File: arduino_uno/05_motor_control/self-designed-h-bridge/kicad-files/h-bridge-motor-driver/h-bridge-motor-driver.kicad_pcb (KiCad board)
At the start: 2 copper layers, 1 part

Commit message: rework pcb
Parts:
- removed REF**: CONN2_2601-3102_WAG, WAGO 2601-3102:CONN2_2601-3102_WAG
- added D1: 1N4007, Diode_THT:D_DO-41_SOD81_P10.16mm_Horizontal, F.Cu at (104.5, 66.8)
- added D2: 1N4007, Diode_THT:D_DO-41_SOD81_P10.16mm_Horizontal, F.Cu at (104.5, 71.0)
- added D3: 1N4007, Diode_THT:D_DO-41_SOD81_P10.16mm_Horizontal, F.Cu at (104.5, 75.3)
- added D4: 1N4007, Diode_THT:D_DO-41_SOD81_P10.16mm_Horizontal, F.Cu at (104.5, 79.5)
- added J1: Conn_01x05_Pin, Connector_PinHeader_2.54mm:PinHeader_1x05_P2.54mm_Vertical, F.Cu at (118.8, 67.0)
- added J3: 2601-3102, WAGO 2601-3102:CONN2_2601-3102_WAG, F.Cu at (108.1, 56.5)
- added J4: 2601-3102, WAGO 2601-3102:CONN2_2601-3102_WAG, F.Cu at (266.0, 53.0)
- added Q1: IRF9540N, Package_TO_SOT_THT:TO-220-3_Vertical, F.Cu at (105.9, 85.6)
- added Q2: IRLIZ44N, Package_TO_SOT_THT:TO-220F-3_Vertical, F.Cu at (119.9, 83.2)
- added Q3: IRF9540N, Package_TO_SOT_THT:TO-220-3_Vertical, F.Cu at (105.9, 91.5)
- added Q4: IRLIZ44N, Package_TO_SOT_THT:TO-220F-3_Vertical, F.Cu at (119.9, 89.5)
- added Q5: BC547, Package_TO_SOT_THT:TO-92_Inline, F.Cu at (123.1, 67.9)
- added Q6: BC547, Package_TO_SOT_THT:TO-92_Inline, F.Cu at (123.1, 73.7)
- added R1: 330, Resistor_THT:R_Axial_DIN0207_L6.3mm_D2.5mm_P10.16mm_Horizontal, F.Cu at (90.9, 52.3)
- added R2: 10k, Resistor_THT:R_Axial_DIN0207_L6.3mm_D2.5mm_P10.16mm_Horizontal, F.Cu at (90.9, 56.3)
- added R3: 10k, Resistor_THT:R_Axial_DIN0207_L6.3mm_D2.5mm_P10.16mm_Horizontal, F.Cu at (90.9, 60.4)
- added R4: 330, Resistor_THT:R_Axial_DIN0207_L6.3mm_D2.5mm_P10.16mm_Horizontal, F.Cu at (90.9, 64.4)
- added R5: 330, Resistor_THT:R_Axial_DIN0207_L6.3mm_D2.5mm_P10.16mm_Horizontal, F.Cu at (90.9, 68.5)
- added R6: 330, Resistor_THT:R_Axial_DIN0207_L6.3mm_D2.5mm_P10.16mm_Horizontal, F.Cu at (90.9, 72.5)
- added R7: 10k, Resistor_THT:R_Axial_DIN0207_L6.3mm_D2.5mm_P10.16mm_Horizontal, F.Cu at (90.9, 76.6)
- added R8: 10k, Resistor_THT:R_Axial_DIN0207_L6.3mm_D2.5mm_P10.16mm_Horizontal, F.Cu at (90.9, 80.6)

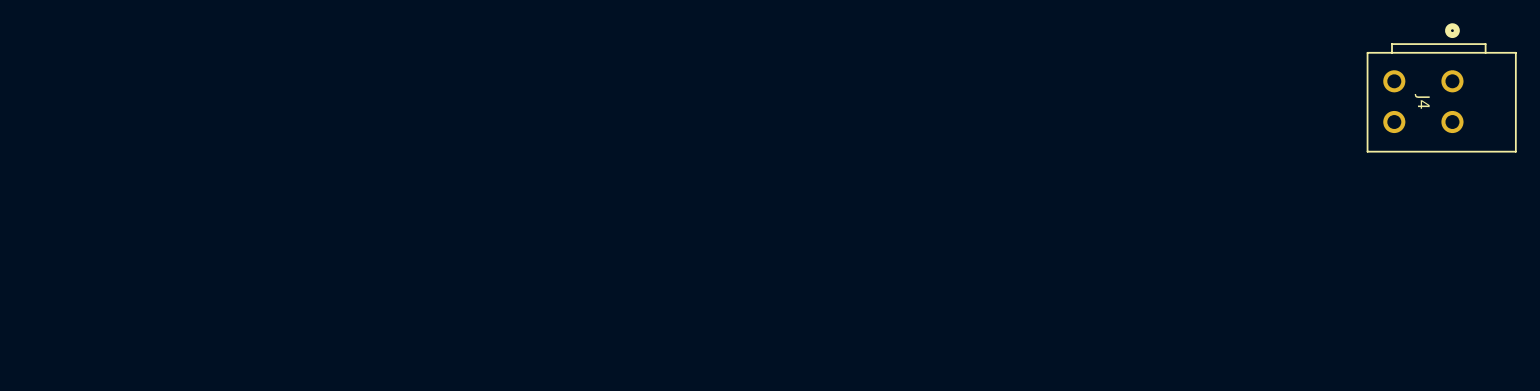
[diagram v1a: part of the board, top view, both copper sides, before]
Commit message: add 3d model to wago connector
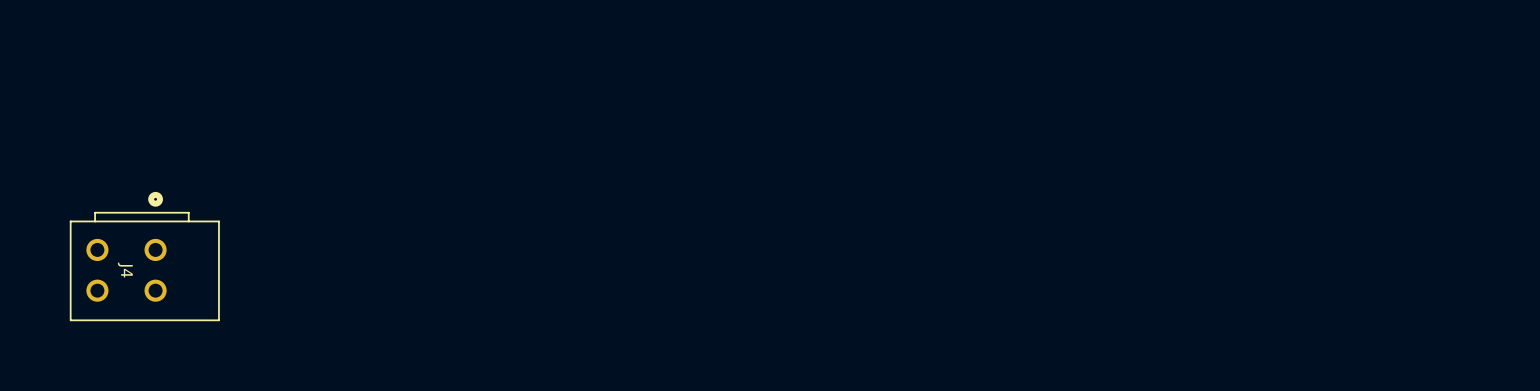
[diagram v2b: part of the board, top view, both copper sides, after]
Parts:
- moved J4 112.4 mm to (154.5, 67.5)
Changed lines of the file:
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@@
 		)
 		(embedded_fonts no)
+		(model "C:/workspace/PycharmProjects/arduino_projects/arduino_uno/05_motor_control/self-designed-h-bridge/kicad-files/part-models/wago-2601-3102/2601-3102.stp"
+			(offset
+				(xyz 4.5 -5 0)
+			)
+			(scale
+				(xyz 1 1 1)
+			)
+			(rotate
+				(xyz -90 -0 90)
+			)
+		)
 	)
 	(footprint "Package_TO_SOT_THT:TO-92_Inline"
@@
 	(footprint "WAGO 2601-3102:CONN2_2601-3102_WAG"
 		(layer "F.Cu")
-		(at 266 53 -90)
+		(at 154.5 67.5 -90)
 		(tags "2601-3102 ")
 		(property "Reference" "J4"
@@
 		)
 		(embedded_fonts no)
+		(model "C:/workspace/PycharmProjects/arduino_projects/arduino_uno/05_motor_control/self-designed-h-bridge/kicad-files/part-models/wago-2601-3102/2601-3102.stp"
+			(offset
+				(xyz 4.5 -5 0)
+			)
+			(scale
+				(xyz 1 1 1)
+			)
+			(rotate
+				(xyz -90 -0 90)
+			)
+		)
 	)
 	(footprint "Package_TO_SOT_THT:TO-220F-3_Vertical"

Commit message: start routing
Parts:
- removed J1: Conn_01x05_Pin, Connector_PinHeader_2.54mm:PinHeader_1x05_P2.54mm_Vertical
- added J2: Conn_01x06_Pin, Connector_PinSocket_2.54mm:PinSocket_1x06_P2.54mm_Vertical, F.Cu at (40.5, 62.5)
- added REF**: MountingHole_3.2mm_M3, MountingHole:MountingHole_3.2mm_M3, F.Cu at (111.0, 34.5)
- added REF**: MountingHole_3.2mm_M3, MountingHole:MountingHole_3.2mm_M3, F.Cu at (110.5, 85.8)
- added REF**: MountingHole_3.2mm_M3, MountingHole:MountingHole_3.2mm_M3, F.Cu at (40.0, 35.5)
- added REF**: MountingHole_3.2mm_M3, MountingHole:MountingHole_3.2mm_M3, F.Cu at (40.5, 85.8)
- moved J4 120.2 mm to (35.5, 50.5), turned to 90 degrees
- moved Q1 61.2 mm to (62.4, 42.5)
- moved Q5 60.6 mm to (62.6, 63.7), turned to -90 degrees
- moved Q2 57.5 mm to (62.4, 84.7)
- moved Q3 51.6 mm to (90.0, 42.5)
- moved R1 45.8 mm to (46.9, 65.0)
- moved D1 43.7 mm to (74.1, 35.5), turned to 180 degrees
- moved R2 43.6 mm to (54.5, 32.4), turned to -90 degrees
- moved D3 41.1 mm to (66.4, 90.8)
- moved D2 35.6 mm to (102.6, 35.5), turned to 180 degrees
- moved Q6 35.1 mm to (90.1, 61.7), turned to -90 degrees
- moved R7 33.8 mm to (58.1, 84.8), turned to 180 degrees
- moved R5 30.1 mm to (62.5, 58.6), turned to 90 degrees
- moved R3 28.9 mm to (83.5, 32.4), turned to -90 degrees
- moved Q4 27.5 mm to (92.9, 84.5)
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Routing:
- net Net-(D1-K): track 0.00 -> 114.9 mm
- net Net-(D1-A): track 0.00 -> 94.4 mm
- net Net-(J2-Pin_5): track 0.00 -> 61.2 mm
- net Net-(D2-A): track 0.00 -> 59.7 mm
- net Net-(J2-Pin_3): track 0.00 -> 44.7 mm
- net Net-(J2-Pin_4): track 0.00 -> 37.7 mm
- net Net-(Q1-G): track 0.00 -> 13.9 mm
- net Net-(Q3-G): track 0.00 -> 11.0 mm
- net Net-(Q6-B): track 0.00 -> 7.06 mm
- net Net-(J2-Pin_2): track 0.00 -> 6.42 mm
- net Net-(Q5-B): track 0.00 -> 5.56 mm
- net Net-(Q5-C): track 0.00 -> 5.21 mm
- net Net-(Q6-C): track 0.00 -> 4.71 mm
